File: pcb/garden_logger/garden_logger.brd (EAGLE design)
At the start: 70 x 70 mm, 40 parts, among them J1 AVR_SPI_PRG_6PTH, J3 RASPBERRYPI-40-PIN-GPIO

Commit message: added buttons and leds.  started laying out board
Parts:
- removed J4: (no value), SparkFun-Connectors:1X02
- added ADC: (no value), SparkFun-Connectors:1X08_ROUND
- added BUTTON, LED: (no value), SparkFun-Connectors:1X03
- added BUTTON1, BUTTON2, BUTTON3: SWITCH-MOMENTARY-2PTH, SparkFun-Electromechanical:TACTILE-PTH
- added ESP-01: (no value), SparkFun-Connectors:1X02
- added LED1, LED2, LED3: (no value), led:CHIPLED_0805
- added R10, R11, R9: 10k, rcl:R0805
- added R6, R7, R8: 330, rcl:R0805
- moved RPI-USART 269.8 mm to (91.4, 47.0)
- moved RPI-I2C 248.3 mm to (87.6, 41.9)
- moved JP5 227.9 mm to (5.08, 76.2)
- moved JP4 221.3 mm to (12.7, 74.9)
- moved L2 211.7 mm to (43.2, 76.2)
- moved L1 206.5 mm to (35.6, 77.5)
- moved R4 206.1 mm to (49.5, 77.5)
- moved R3 204.7 mm to (55.9, 77.5)
- moved R2 204.7 mm to (62.2, 78.7)
- moved JP3 203.9 mm to (73.7, 76.2)
- moved LOGO1 202.9 mm to (8.89, 81.3)
- moved R5 200.2 mm to (30.5, 76.2)
- moved C5 197.0 mm to (85.1, 78.7)
- moved AREF 187.7 mm to (67.3, 78.7)
- moved USART0 146.2 mm to (30.5, 81.3)
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- renumbered J2 to PE
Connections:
- new net N$11: LED1.C, R6.2
- new net N$14: LED2.C, R7.2
- new net N$15: LED3.C, R8.2
- new net N$16: LED.1, LED1.A
- new net N$17: LED.2, LED2.A
- new net N$18: LED.3, LED3.A
- new net N$20: BUTTON.3, BUTTON3.3, R11.2
- new net N$21: BUTTON.2, BUTTON2.3, R10.2
- new net N$22: BUTTON.1, BUTTON1.3, R9.2
- net GND: now also BUTTON1.1, BUTTON2.1, BUTTON3.1, R6.1, R7.1, R8.1
- net N$6: now also ESP-01.1; no longer J4.1
- net N$7: now also ESP-01.2; no longer J4.2
- net PC0: now also ADC.1
- net PC1: now also ADC.2
- net PC2: now also ADC.3
- net PC3: now also ADC.4
- net PC4: now also ADC.5
- net PC5: now also ADC.6
- net PE2: now also ADC.7
- net PE3: now also ADC.8
- net VCC: now also R10.1, R11.1, R9.1
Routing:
- added copper zone on layer 16, net GND

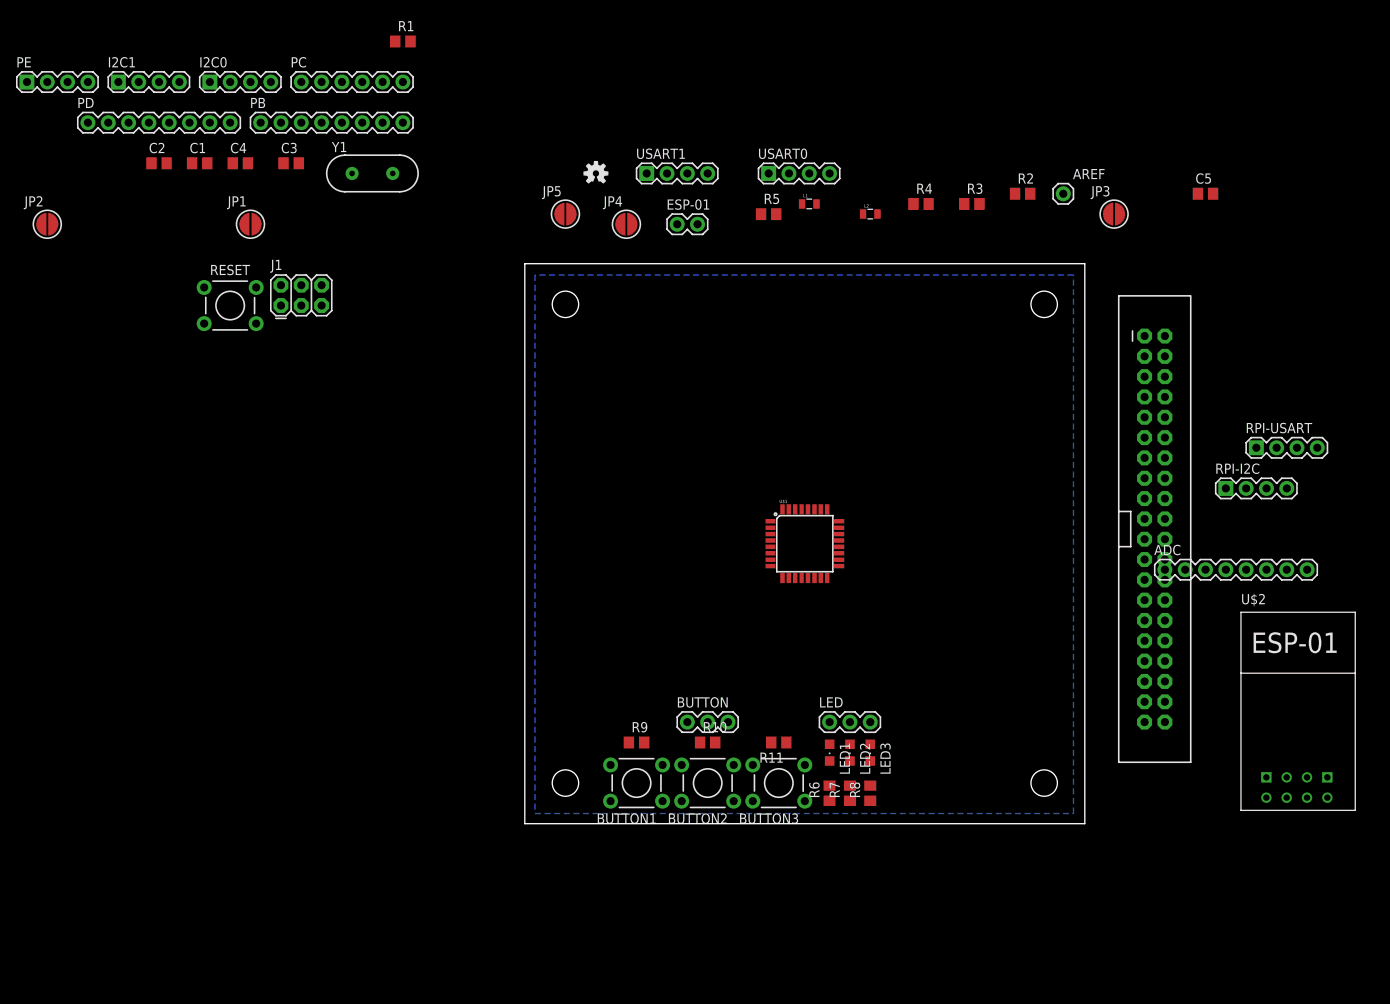
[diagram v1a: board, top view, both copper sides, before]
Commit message: removed rpi header to have bigger proto area.  Mostly done routeing
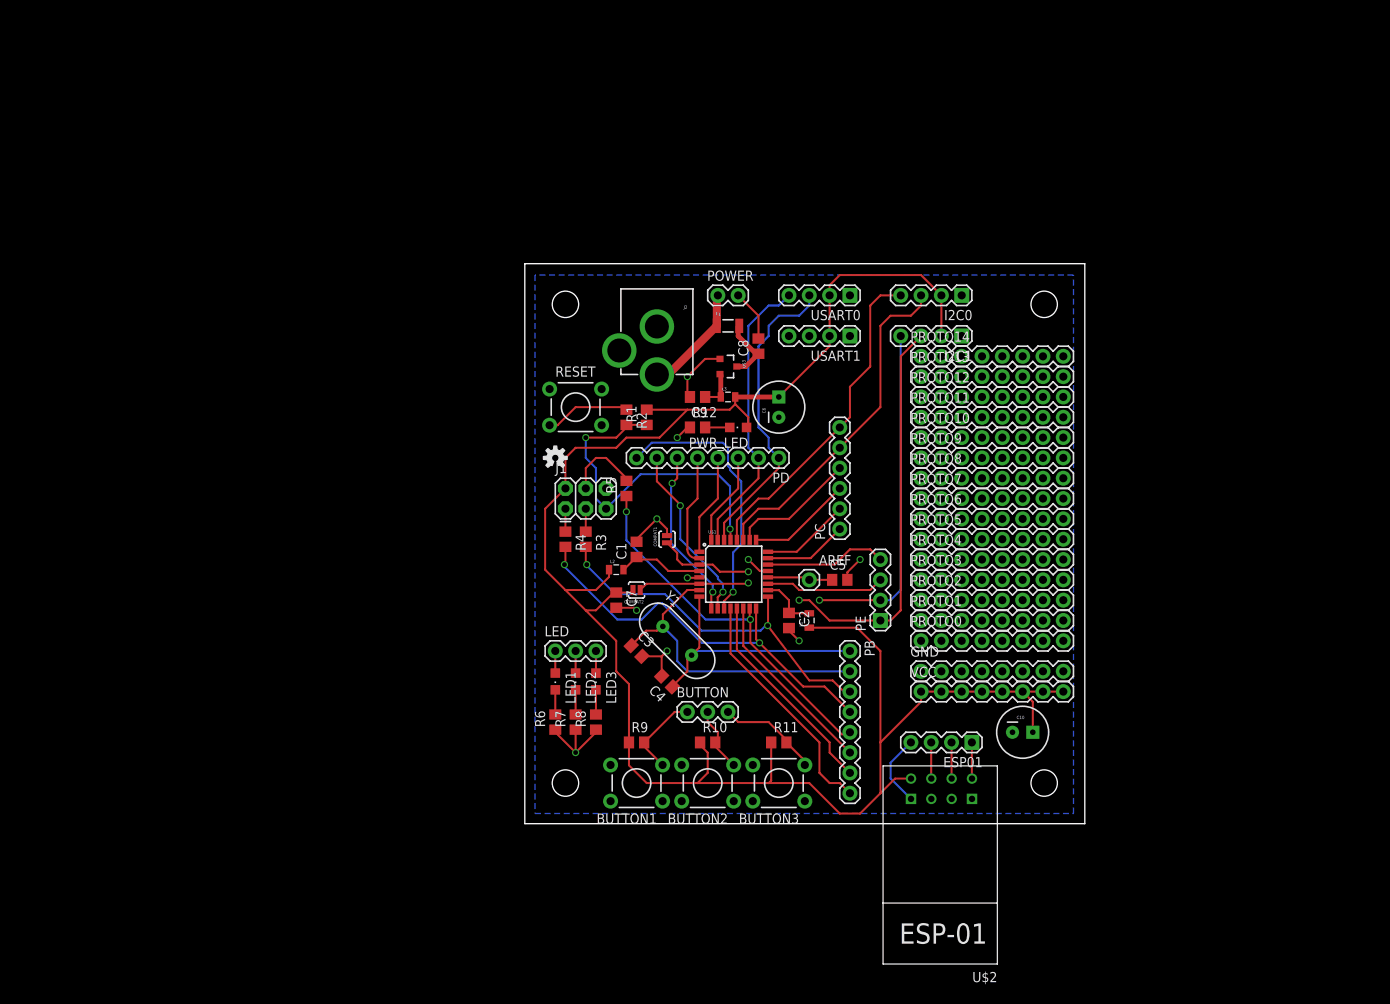
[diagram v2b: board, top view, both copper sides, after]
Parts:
- removed ADC: (no value), SparkFun-Connectors:1X08_ROUND
- removed ESP-01: (no value), SparkFun-Connectors:1X02
- removed J3: RASPBERRYPI-40-PIN-GPIO, SparkFun-Boards:2X20-SHROUDED
- removed JP1, JP2, JP3, JP4, JP5: JUMPER-PAD-2-NOROUND, SparkFun-Passives:PAD-JUMPER-2-NO_YES_SILK_ROUND
- removed RPI-I2C, RPI-USART: (no value), SparkFun-Connectors:1X04
- added C10, C6: 100uF, SparkFun-Passives:CPOL-RADIAL-100UF-25V
- added C7: .1uF, rcl:C0805
- added C8, C9: 1uF, rcl:C0805
- added COMPAT1, COMPAT2: SOLDERJUMPER-OLDNO, SparkFun-Retired:SJ_2S-NO
- added ESP01: (no value), SparkFun-Connectors:1X04
- added F1: PTCSMD, SparkFun-PowerIC:PTC-1206
- added GND, PROTO0, PROTO1, PROTO10, PROTO11, PROTO12, PROTO13, PROTO14, PROTO2, PROTO3, PROTO4, PROTO5, PROTO6, PROTO7, PROTO8, PROTO9, VCC: (no value), SparkFun-Connectors:1X08_ROUND
- added J2: POWER_JACKPTH, SparkFun-Connectors:POWER_JACK_PTH
- added L3: 10uH, SparkFun-Passives:0805
- added POWER: (no value), SparkFun-Connectors:1X02
- added PWR_LED: (no value), led:CHIPLED_0805
- added R12: 330, rcl:R0805
- added U$3: MCP1702, zjembedded_eagle:SOT23-3
- moved PE 126.1 mm to (44.5, 25.4), turned to 90 degrees
- moved I2C1 110.1 mm to (54.6, 61.0), turned to 180 degrees
- moved PB 98.9 mm to (40.6, 21.6), turned to 270 degrees
- moved I2C0 97.7 mm to (54.6, 66.0), turned to 180 degrees
- moved C2 97.3 mm to (33.0, 25.4), turned to 270 degrees
- moved PD 96.0 mm to (31.8, 45.7), turned to 180 degrees
- moved PC 87.5 mm to (39.4, 36.8), turned to 90 degrees
- moved C4 83.9 mm to (17.8, 17.8), turned to 135 degrees
- moved C3 74.7 mm to (14.0, 21.6), turned to 315 degrees
- moved C1 72.9 mm to (14.0, 34.3), turned to 90 degrees
- moved Y1 69.7 mm to (19.1, 22.9), turned to 315 degrees
- moved C5 66.5 mm to (39.4, 30.5)
- moved R3 63.9 mm to (7.62, 35.6), turned to 270 degrees
- moved R4 61.1 mm to (5.08, 35.6), turned to 270 degrees
- moved AREF 57.8 mm to (35.6, 30.5)
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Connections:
- removed net 3.3V: J3.1, J3.17
- removed net 5V: J3.2, J3.4
- new net N$10: F1.1, J2.PWR, POWER.1
- new net N$19: C9.1, L3.1, U$3.2
- net GND: now also C10.2, C6.2, C7.2, C8.2, C9.2, COMPAT1.2, GND.1, GND.2, GND.3, GND.4, GND.5, GND.6, GND.7, GND.8, J2.GND, J2.GNDBREAK, POWER.2, R12.1, U$3.1; no longer J3.14, J3.20, J3.25, J3.30, J3.34, J3.39, J3.6, J3.9, JP1.2, RPI-I2C.1, RPI-USART.1
- net N$1: no longer JP3.1
- net N$12: now also ESP01.3, U$2.RST; no longer J3.5, RPI-I2C.4
- net N$13: now also ESP01.4, U$2.RX; no longer J3.3, RPI-I2C.3
- net N$6: now also ESP01.1, U$2.TX; no longer ESP-01.1, JP5.2, U$2.CH_PD
- net N$7: now also ESP01.2, U$2.CH_PD; no longer ESP-01.2, JP4.1, U$2.RST
- net N$8: now also C8.1, F1.2, U$3.3; no longer J3.8, RPI-USART.4
- net N$9: now also PWR_LED.C, R12.2; no longer J3.10, RPI-USART.3
- net PB3: no longer USART1.3
- net PB4: now also USART1.3
- net PC0: no longer ADC.1
- net PC1: no longer ADC.2
- net PC2: no longer ADC.3
- net PC3: now also PC.4; no longer ADC.4
- net PC4: now also PC.5; no longer ADC.5
- net PC5: no longer ADC.6
- net PD0: no longer U$2.TX
- net PD1: no longer U$2.RX
- net PD6: no longer JP5.1
- net PD7: no longer JP4.2
- net PE0: now also COMPAT1.1; no longer JP1.1
- net PE1: now also COMPAT2.1; no longer JP2.1
- net PE2: no longer ADC.7
- net PE3: no longer ADC.8
- net VCC: now also C10.1, C6.1, C7.1, COMPAT2.2, L3.2, PWR_LED.A, VCC.1, VCC.2, VCC.3, VCC.4, VCC.5, VCC.6, VCC.7, VCC.8; no longer JP2.2, JP3.2, RPI-I2C.2, RPI-USART.2
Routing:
- net VCC: track 0.00 -> 245.1 mm
- net PE0: track 0.00 -> 61.8 mm, vias 0 -> 2
- net PE1: track 0.00 -> 56.3 mm, vias 0 -> 2
- net GND: track 0.00 -> 51.9 mm, vias 0 -> 10
- net PB4: track 0.00 -> 51.9 mm, vias 0 -> 2
- net PB3: track 0.00 -> 46.7 mm, vias 0 -> 2
- net PB5: track 0.00 -> 46.6 mm, vias 0 -> 2
- net PC6: track 0.00 -> 43.0 mm, vias 0 -> 2
- net PC4: track 0.00 -> 42.7 mm
- net PC5: track 0.00 -> 41.3 mm
- net PB6: track 0.00 -> 39.5 mm
- net PD0: track 0.00 -> 38.6 mm
- net PD1: track 0.00 -> 36.0 mm
- net PD7: track 0.00 -> 34.1 mm, vias 0 -> 1
- net PB7: track 0.00 -> 32.7 mm
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
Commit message: finished routing.  working on labels
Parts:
- removed ESP01: (no value), SparkFun-Connectors:1X04
- added J3: (no value), SparkFun-Connectors:1X05
- added VRAW: (no value), SparkFun-Connectors:1X01
- moved F1 3.59 mm to (21.8, 61.7)
- moved POWER 3.57 mm to (20.6, 65.8)
- moved J2 2.79 mm to (13.7, 69.8)
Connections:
- new net N$23: J3.1, U$2.RX
- net N$12: now also J3.3, U$2.CH_PD; no longer ESP01.3, U$2.RST
- net N$13: now also J3.2, U$2.TX; no longer ESP01.4, U$2.RX
- net N$6: now also J3.5, U$2.VCC; no longer ESP01.1, U$2.TX
- net N$7: now also J3.4, U$2.RST; no longer ESP01.2, U$2.CH_PD
- net N$8: now also VRAW.1
- net VCC: no longer U$2.VCC
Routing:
- net PB4: track 51.9 -> 99.0 mm
- net PB3: track 46.7 -> 85.2 mm
- net N$23: track 0.00 -> 20.7 mm
- net PE1: track 56.3 -> 67.6 mm
- net PE0: track 61.8 -> 69.6 mm
- net N$8: track 8.15 -> 15.9 mm
- net N$13: track 9.17 -> 4.27 mm
- net VCC: track 245.1 -> 240.5 mm
- net GND: track 51.9 -> 48.8 mm, vias 10 -> 11
- net N$10: track 13.9 -> 13.2 mm

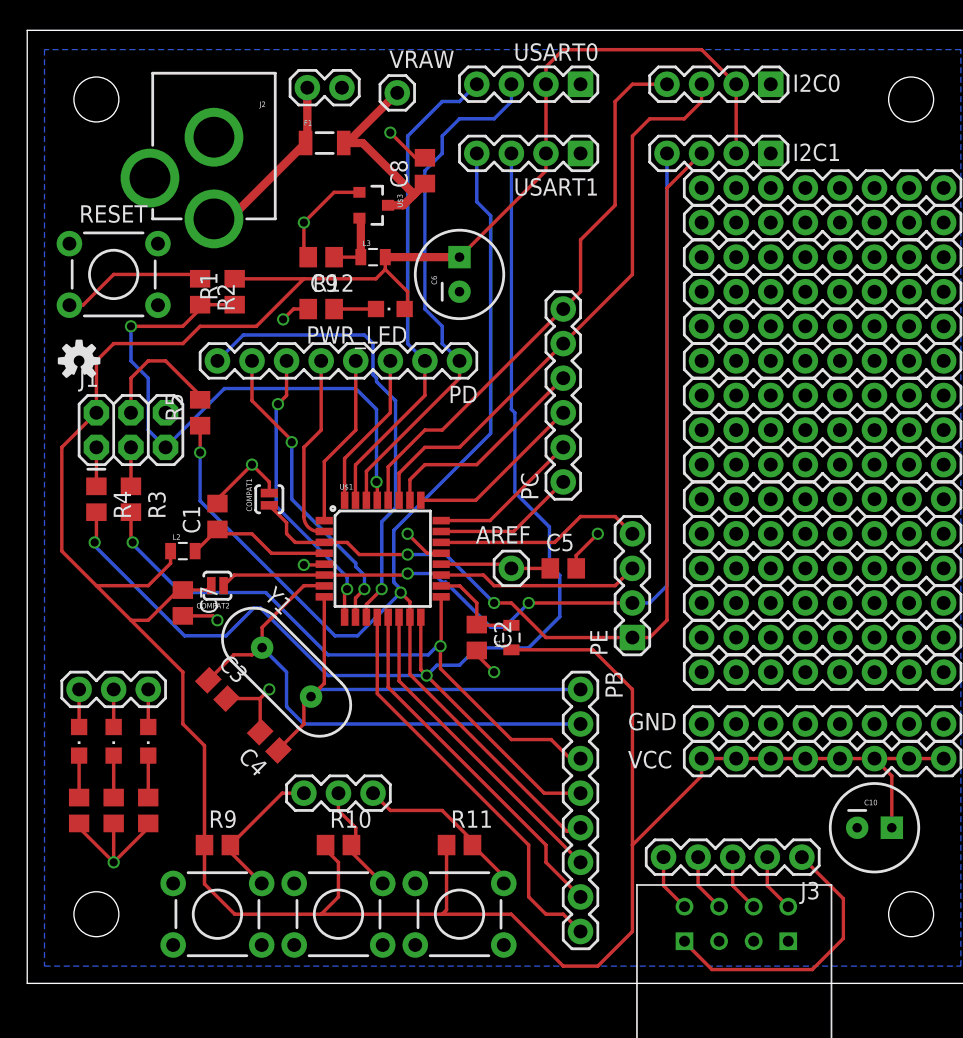
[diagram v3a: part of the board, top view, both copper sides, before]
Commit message: done with pcb labels
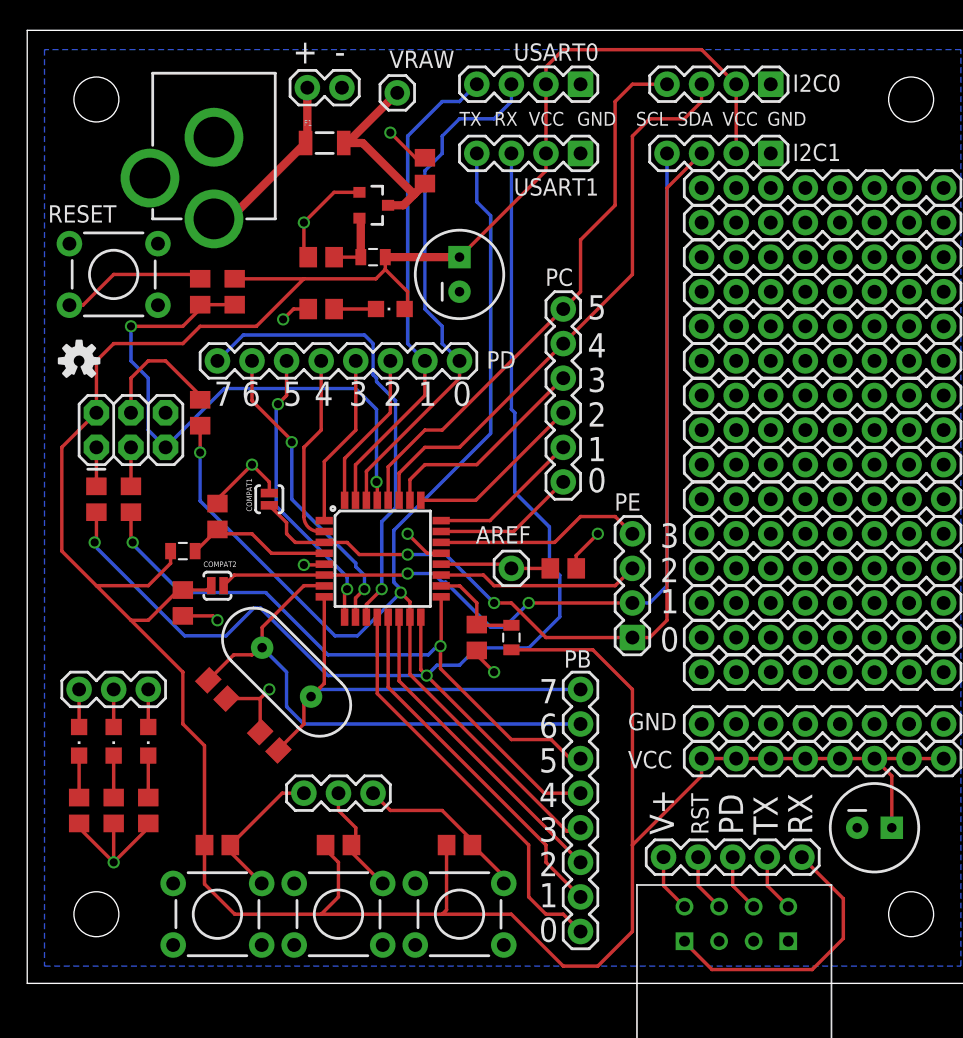
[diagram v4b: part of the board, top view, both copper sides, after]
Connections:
- net N$12 renamed ESP01_CH_PD
- net N$13 renamed ESP01_TXD
- net N$23 renamed ESP01_RXD
- net N$6 renamed ESP01_VCC
- net N$7 renamed ESP01_RST
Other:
- board text added: "+"
- board text added: "-"
- board text added: "0"
- board text added: "1"
- board text added: "2"
- board text added: "3"
- board text added: "4"
- board text added: "5"
- board text added: "6"
- board text added: "7"
- board text added: "GND"
- board text added: "PD"
- board text added: "RST"
- board text added: "RX"
- board text added: "SCL"
- board text added: "SDA"
- board text added: "TX"
- board text added: "V+"
- board text added: "VCC"
